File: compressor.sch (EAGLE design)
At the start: 51 parts, among them U1 MAX5419LETA+, U2 MAX5419LETA+, X1 OPAMP, X10 OPAMP, X2 OPAMP, X3 OPAMP, X5 OPAMP, X6 OPAMP, X7 OPAMP, X8 OPAMP, X9 OPAMP

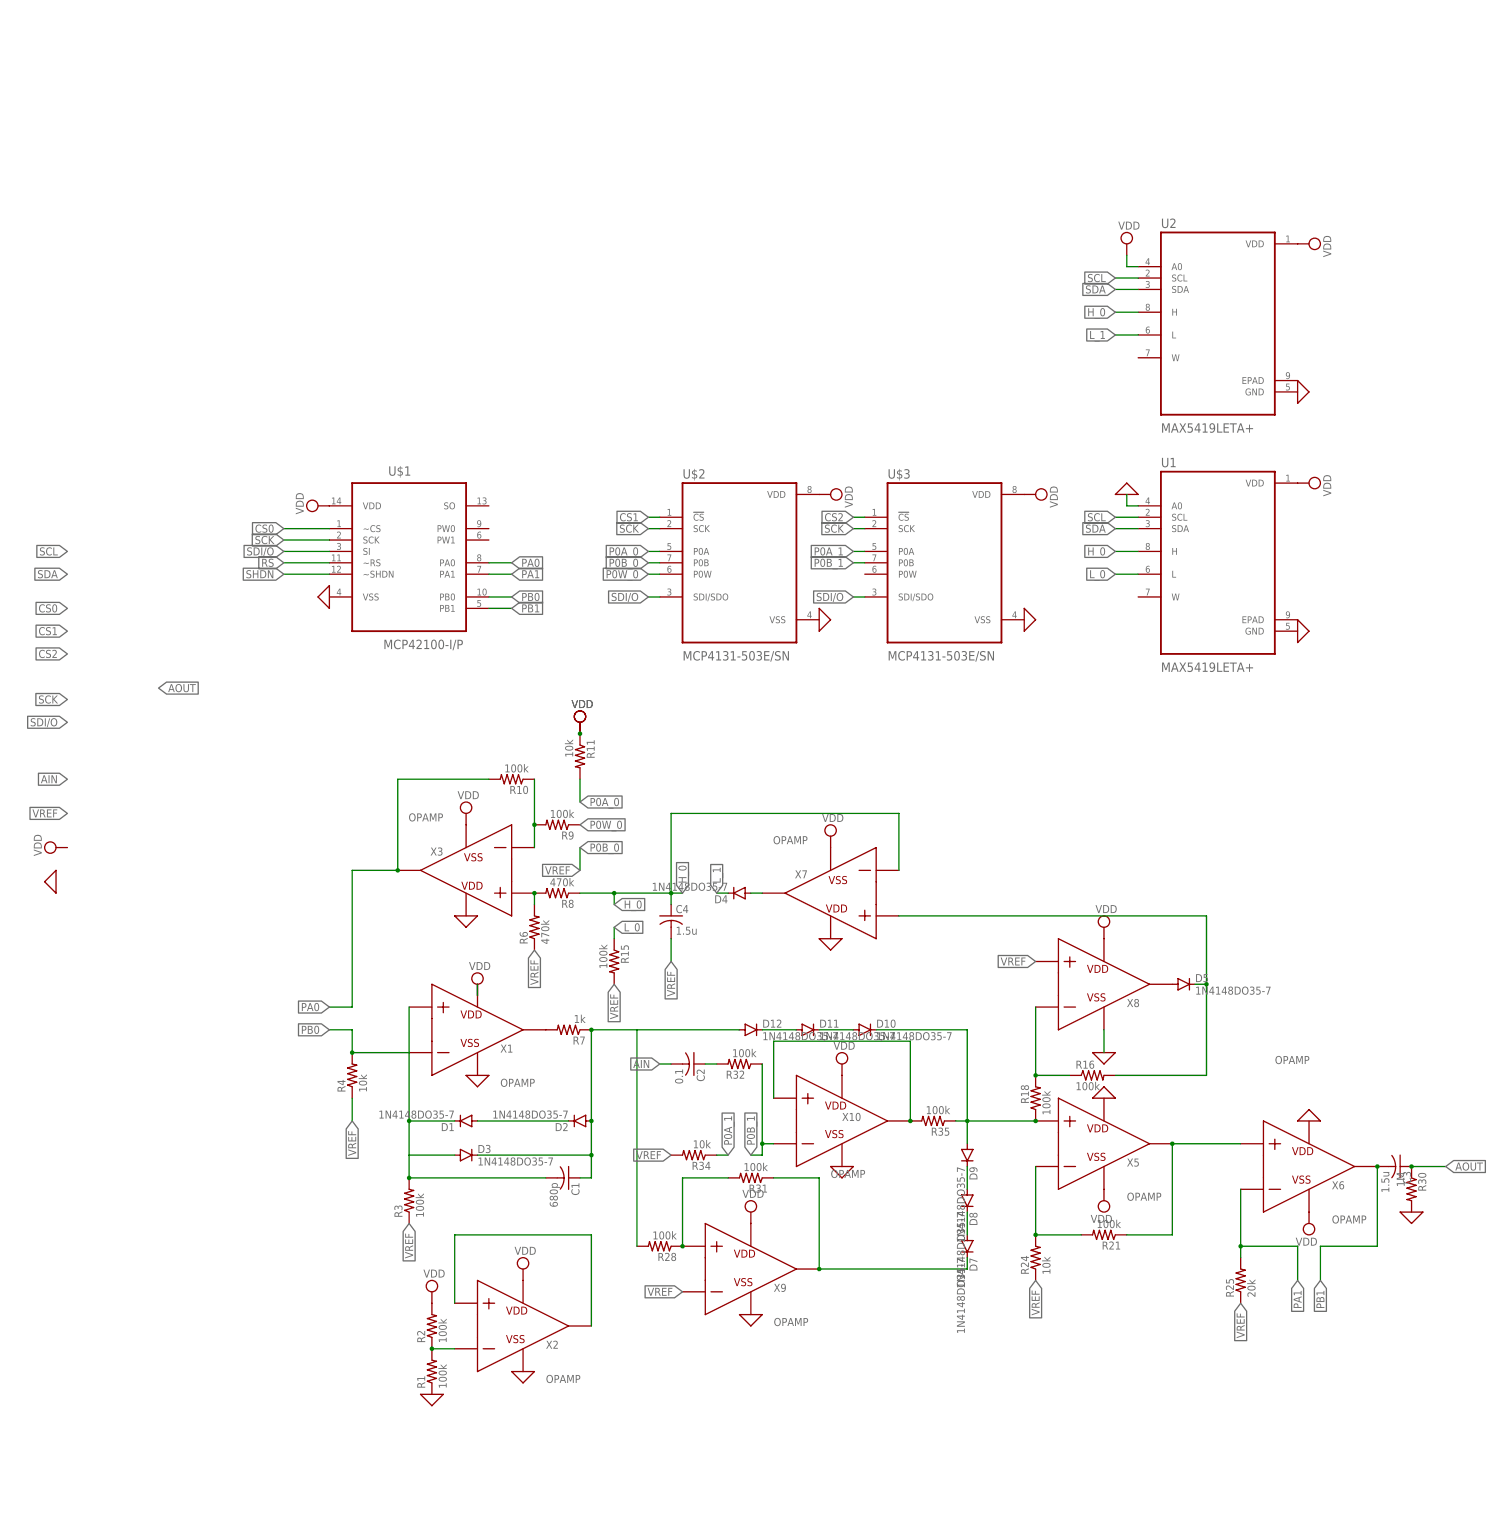
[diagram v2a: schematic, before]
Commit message: update, split out into schematics for each component
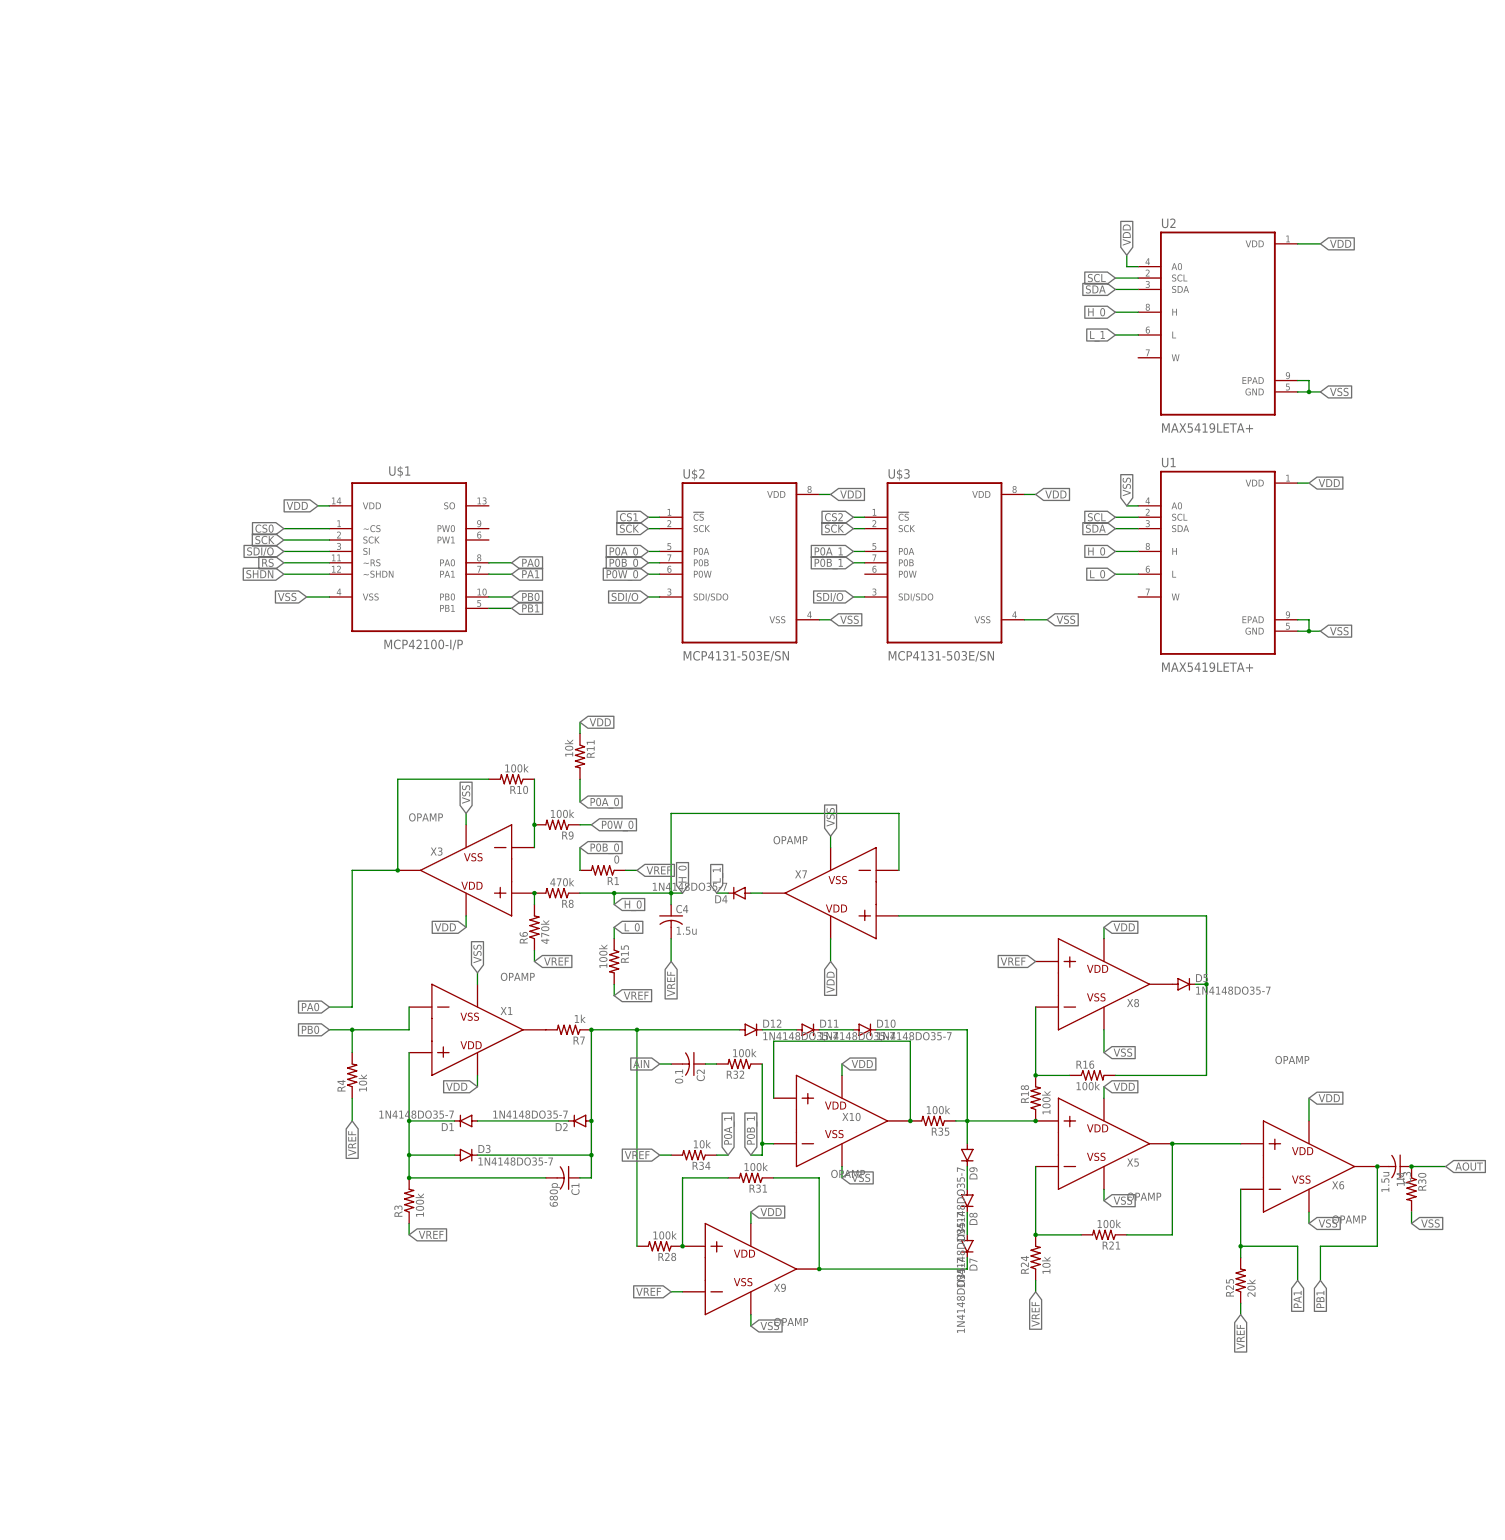
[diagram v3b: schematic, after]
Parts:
- removed R2: 100k, rcl:R-US_0204/7
- removed X2: OPAMP, ngspice-simulation:OPAMP
- C1, C2, C3, C4: device rcl:C-US025-024X044 -> rcl:C-USC0402
- R1: value 100k -> 0; device rcl:R-US_0204/7 -> rcl:R-US_R0402
- R10, R11, R15, R16, R18, R21, R24, R25, R28, R3, R30, R31, R32, R34, R35, R4, R6, R7, R8, R9: device rcl:R-US_0204/7 -> rcl:R-US_R0402
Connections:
- removed net 0: R1.1, R30.2, U$1.VSS, U$2.VSS, U$3.VSS, U1.A0, U1.GND, U2.GND, X1.VSS, X10.VSS, X2.VSS, X3.VDD, X5.VDD, X6.VDD, X7.VDD, X8.VSS, X9.VSS
- removed net N$10: R11.2
- removed net N$11: C4.2
- removed net N$4: R1.2, R2.1, X2.N
- removed net N$5: X2.P, X2.VOUT
- new net VSS: R30.2, U$1.VSS, U$2.VSS, U$3.VSS, U1.A0, U1.EPAD, U1.GND, U2.EPAD, U2.GND, X1.VSS, X10.VSS, X3.VSS, X5.VSS, X6.VSS, X7.VSS, X8.VSS, X9.VSS
- net P0A_0: now also R11.2
- net P0B_0: now also R1.2
- net P0W_0: now also R9.1
- net VDD: now also X3.VDD, X5.VDD, X6.VDD, X7.VDD; no longer R2.2, X2.VDD, X3.VSS, X5.VSS, X6.VSS, X7.VSS
- net VREF: now also C4.2, R1.1, R15.2, R24.1, R25.1, R3.1, R34.2, R6.1, X9.N
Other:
- moved on the sheet: R1, X1

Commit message: rm cache files, add boards for components
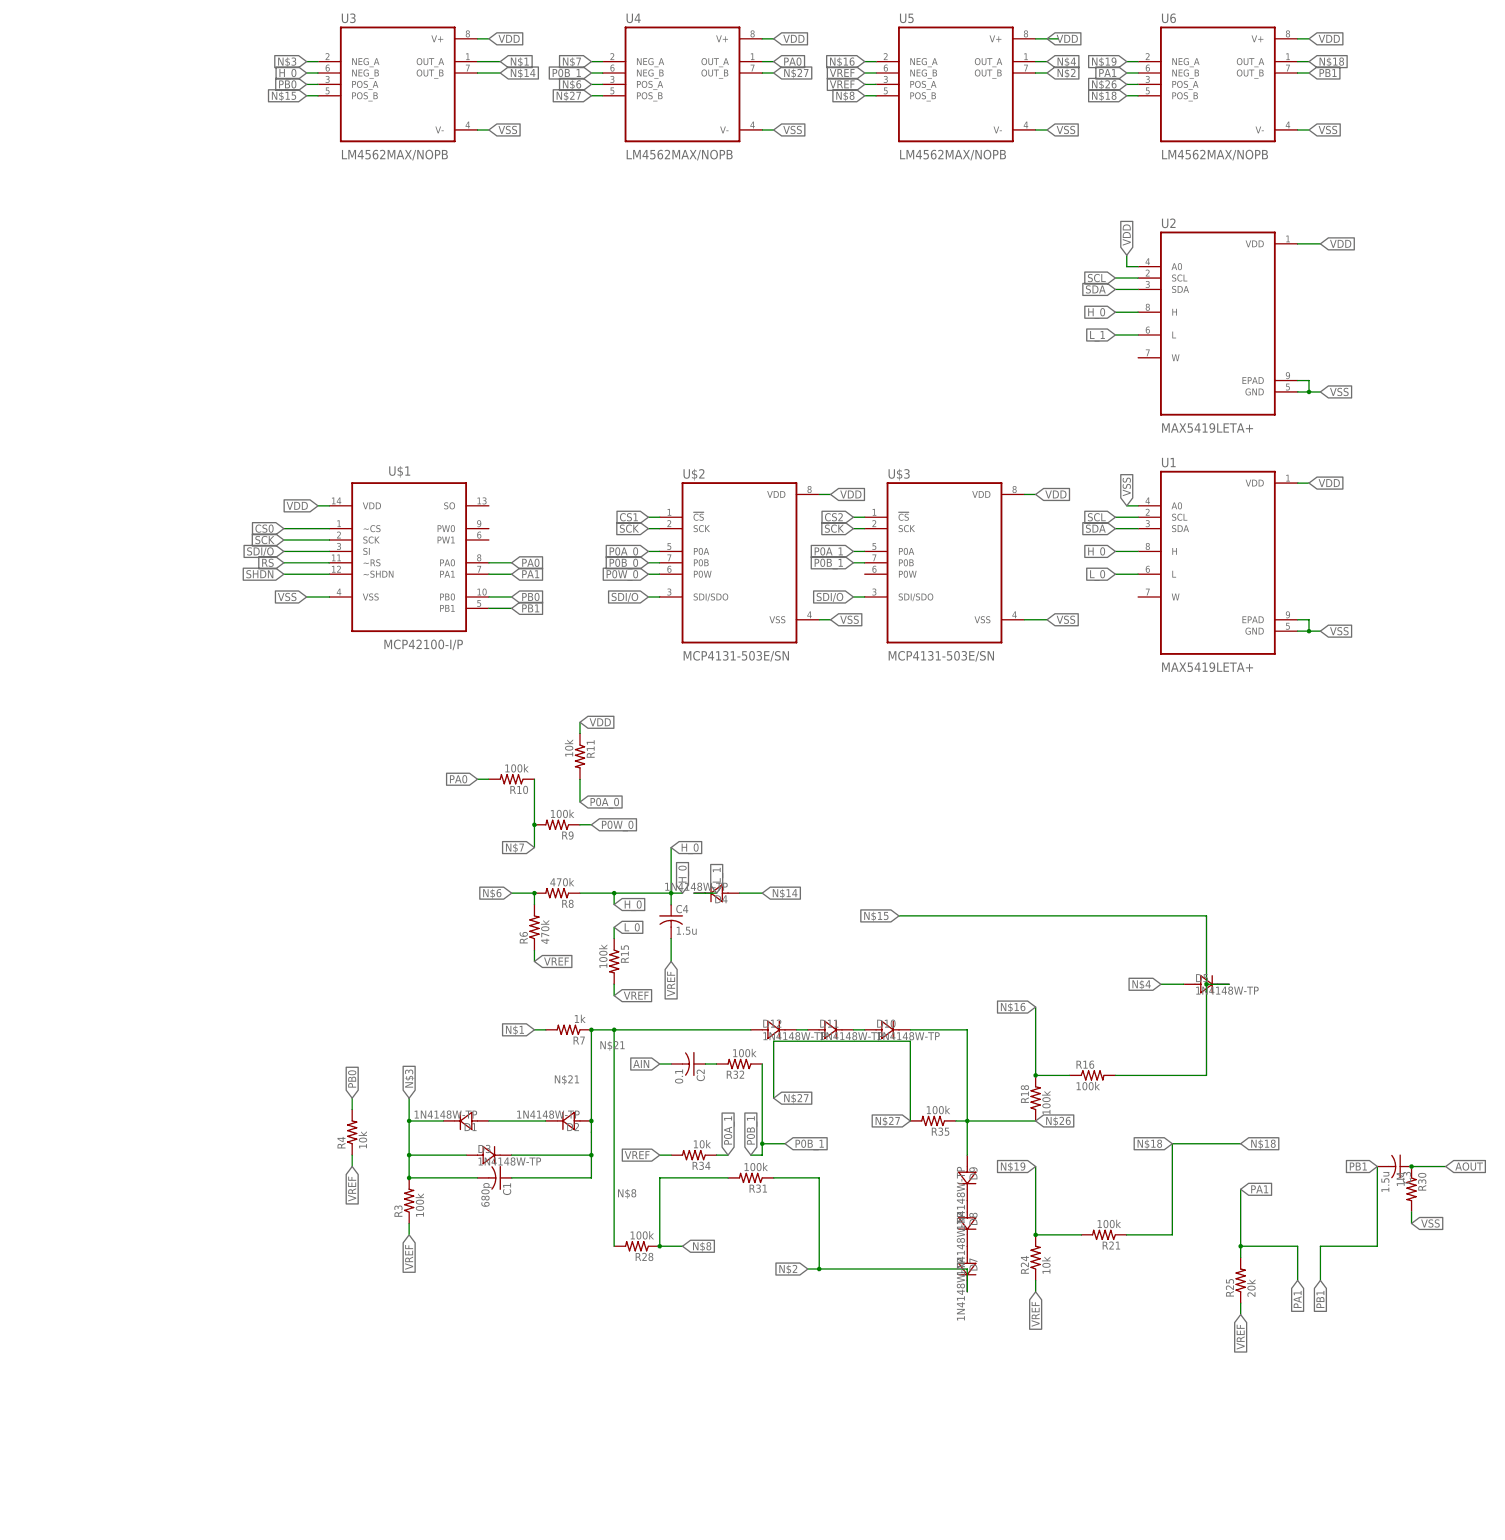
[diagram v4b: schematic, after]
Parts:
- removed R1: 0, rcl:R-US_R0402
- removed X1, X10, X3, X5, X6, X7, X8, X9: OPAMP, ngspice-simulation:OPAMP
- added U3, U4, U5, U6: LM4562MAX/NOPB, LM4562MAX_NOPB:LM4562MAX/NOPB
- D1, D10, D11, D12, D2, D3, D4, D5, D7, D8, D9: value 1N4148DO35-7 -> 1N4148W-TP; device diode:1N4148DO35-7 -> 1N4148W-TP:1N4148W-TP
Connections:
- removed net N$22: R28.1, R31.2, X9.P
- removed net N$23: D7.C, R31.1, X9.VOUT
- removed net N$33: D5.A, X8.VOUT
- new net N$2: D7.C, R31.1, U5.OUT_B
- new net N$4: D5.A, U5.OUT_A
- new net N$8: R28.1, R31.2, U5.POS_B
- net H_0: now also U3.NEG_B; no longer X7.N
- net N$1: now also U3.OUT_A; no longer X1.VOUT
- net N$14: now also U3.OUT_B; no longer X7.VOUT
- net N$15: now also U3.POS_B; no longer X7.P
- net N$16: now also U5.NEG_A; no longer X8.N
- net N$18: now also U6.OUT_A, U6.POS_B; no longer X5.VOUT, X6.P
- net N$19: now also U6.NEG_A; no longer X5.N
- net N$26: now also U6.POS_A; no longer X5.P
- net N$27: now also U4.OUT_B, U4.POS_B; no longer X10.P, X10.VOUT
- net N$3: now also U3.NEG_A; no longer X1.P
- net N$6: now also U4.POS_A; no longer X3.P
- net N$7: now also U4.NEG_A; no longer X3.N
- net P0B_0: no longer R1.2
- net P0B_1: now also U4.NEG_B; no longer X10.N
- net PA0: now also U4.OUT_A; no longer X3.VOUT
- net PA1: now also U6.NEG_B; no longer X6.N
- net PB0: now also U3.POS_A; no longer X1.N
- net PB1: now also U6.OUT_B; no longer X6.VOUT
- net VDD: now also U3.V+, U4.V+, U5.V+, U6.V+; no longer X1.VDD, X10.VDD, X3.VDD, X5.VDD, X6.VDD, X7.VDD, X8.VDD, X9.VDD
- net VREF: now also U5.NEG_B, U5.POS_A; no longer R1.1, X9.N
- net VSS: now also U3.V-, U4.V-, U5.V-, U6.V-; no longer X1.VSS, X10.VSS, X3.VSS, X5.VSS, X6.VSS, X7.VSS, X8.VSS, X9.VSS
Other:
- moved on the sheet: C1, R28, R4
